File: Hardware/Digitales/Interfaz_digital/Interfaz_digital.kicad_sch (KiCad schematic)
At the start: 42 parts, among them J0 Screw_Terminal_01x09, J1-1 Screw_Terminal_01x01, J1-2 Screw_Terminal_01x01, J2-1 Screw_Terminal_01x01, J2-2 Screw_Terminal_01x01, J3-1 Screw_Terminal_01x01, J3-2 Screw_Terminal_01x01, J4-1 Screw_Terminal_01x01, J4-2 Screw_Terminal_01x01, J5-1 Screw_Terminal_01x01, J5-2 Screw_Terminal_01x01, J6-1 Screw_Terminal_01x01, J6-2 Screw_Terminal_01x01, J7-1 Screw_Terminal_01x01, J7-2 Screw_Terminal_01x01, J8-1 Screw_Terminal_01x01, J8-2 Screw_Terminal_01x01, J9 Screw_Terminal_01x10, U1 TLP521-1, U2 TLP521-1, U3 TLP521-1, U4 TLP521-1, U5 TLP521-1, U6 TLP521-1, U7 TLP521-1, U8 TLP521-1

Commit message: Referencias a los componentes de los circuitos
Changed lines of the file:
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@@
 	(text "Interfaz de señales digitales"
 		(exclude_from_sim no)
-		(at 212.344 172.72 0)
+		(at 235.204 173.228 0)
 		(effects
 			(font
@@
 			)
 		)
-		(property "Datasheet" "https://www.alldatasheet.com/html-pdf/32438/TOSHIBA/TLP521/245/1/TLP521.html"
+		(property "Datasheet" "https://docs.rs-online.com/d620/0900766b800287f7.pdf"
 			(at 160.02 102.87 0)
 			(effects
@@
 			)
 		)
-		(property "Datasheet" "https://www.alldatasheet.com/html-pdf/32438/TOSHIBA/TLP521/245/1/TLP521.html"
+		(property "Datasheet" "https://docs.rs-online.com/d620/0900766b800287f7.pdf"
 			(at 160.02 68.58 0)
 			(effects
@@
 			)
 		)
-		(property "Datasheet" "https://www.alldatasheet.com/html-pdf/32438/TOSHIBA/TLP521/245/1/TLP521.html"
+		(property "Datasheet" "https://docs.rs-online.com/d620/0900766b800287f7.pdf"
 			(at 160.02 156.21 0)
 			(effects
@@
 			)
 		)
-		(property "Datasheet" "https://www.alldatasheet.com/html-pdf/32438/TOSHIBA/TLP521/245/1/TLP521.html"
+		(property "Datasheet" "https://docs.rs-online.com/d620/0900766b800287f7.pdf"
 			(at 160.02 138.43 0)
 			(effects
@@
 			)
 		)
-		(property "Datasheet" "https://www.alldatasheet.com/html-pdf/32438/TOSHIBA/TLP521/245/1/TLP521.html"
+		(property "Datasheet" "https://docs.rs-online.com/d620/0900766b800287f7.pdf"
 			(at 160.02 33.02 0)
 			(effects
@@
 			)
 		)
-		(property "Datasheet" "https://www.alldatasheet.com/html-pdf/32438/TOSHIBA/TLP521/245/1/TLP521.html"
+		(property "Datasheet" "https://docs.rs-online.com/d620/0900766b800287f7.pdf"
 			(at 160.02 50.8 0)
 			(effects
@@
 			)
 		)
-		(property "Datasheet" "https://www.alldatasheet.com/html-pdf/32438/TOSHIBA/TLP521/245/1/TLP521.html"
+		(property "Datasheet" "https://docs.rs-online.com/d620/0900766b800287f7.pdf"
 			(at 160.02 120.65 0)
 			(effects
@@
 			)
 		)
-		(property "Datasheet" "https://www.alldatasheet.com/html-pdf/32438/TOSHIBA/TLP521/245/1/TLP521.html"
+		(property "Datasheet" "https://docs.rs-online.com/d620/0900766b800287f7.pdf"
 			(at 160.02 86.36 0)
 			(effects

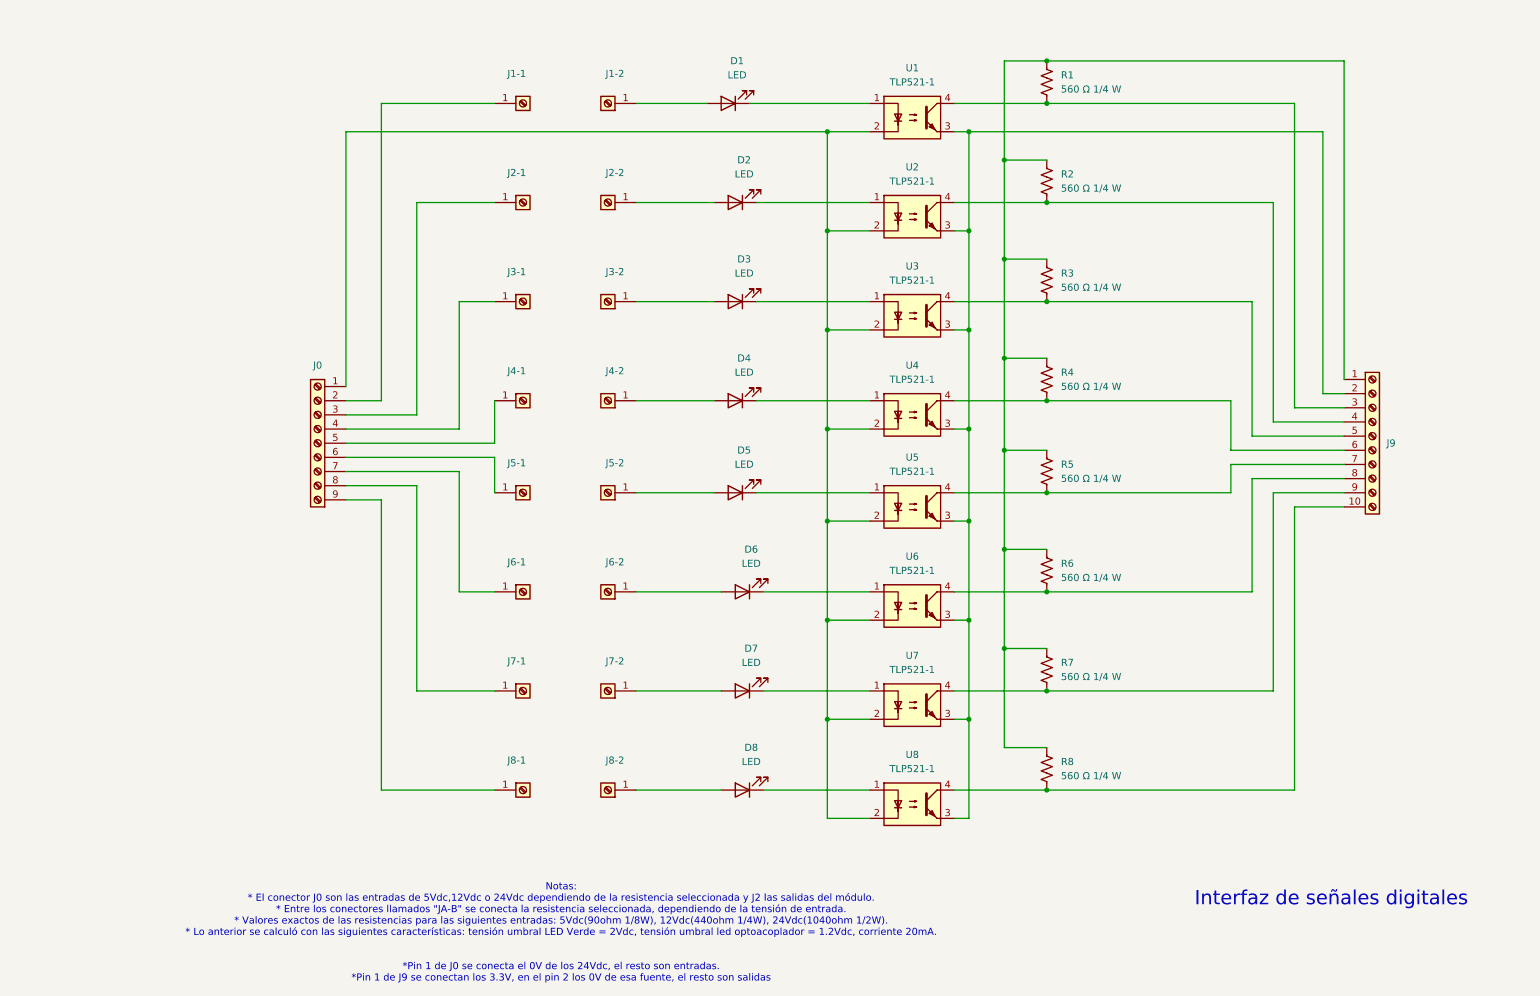
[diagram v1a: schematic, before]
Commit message: Corrección para el mensaje de alerta en estado manual
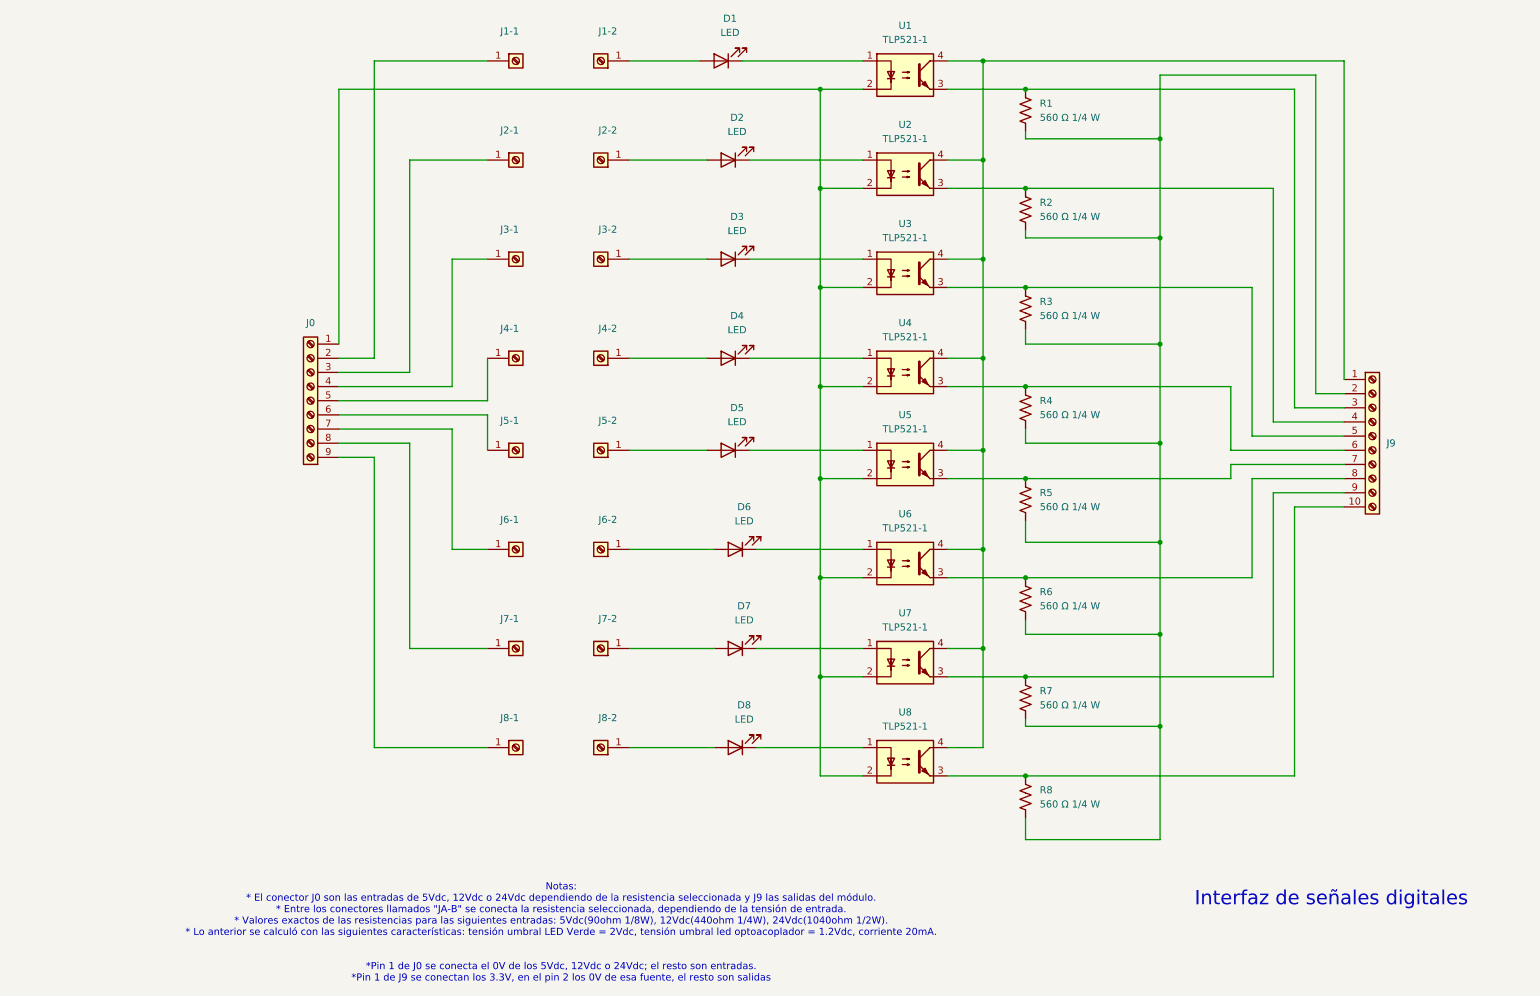
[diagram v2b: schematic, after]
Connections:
- new net: J9.7 (Pin_7), R5.1, U5.3
- new net: J9.1 (Pin_1), U1.4, U2.4, U3.4, U4.4, U5.4, U6.4, U7.4, U8.4
- new net: J9.5 (Pin_5), R3.1, U3.3
- new net: J9.10 (Pin_10), R8.1, U8.3
- new net: J9.2 (Pin_2), R1.2, R2.2, R3.2, R4.2, R5.2, R6.2, R7.2, R8.2
- new net: J9.8 (Pin_8), R6.1, U6.3
- new net: J9.9 (Pin_9), R7.1, U7.3
- new net: J9.3 (Pin_3), R1.1, U1.3
- new net: J9.4 (Pin_4), R2.1, U2.3
- new net: J9.6 (Pin_6), R4.1, U4.3
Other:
- note added: "Notas: * El conector J0 son las entradas de 5Vdc, 12Vdc o 24Vdc dependiendo de la resistencia seleccionada y J9 las salidas del módulo. * Entre los conectores llamados "JA-B" se conecta la resistencia seleccionada, dependiendo de la tensión de entrada. * Valores exactos de las resistencias para las siguientes entradas: 5Vdc(90ohm 1/8W), 12Vdc(440ohm 1/4W), 24Vdc(1040ohm 1/2W). * Lo anterior se ca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"
- note removed: "Notas: * El conector J0 son las entradas de 5Vdc,12Vdc o 24Vdc dependiendo de la resistencia seleccionada y J2 las salidas del módulo. * Entre los conectores llamados "JA-B" se conecta la resistencia seleccionada, dependiendo de la tensión de entrada. * Valores exactos de las resistencias para las siguientes entradas: 5Vdc(90ohm 1/8W), 12Vdc(440ohm 1/4W), 24Vdc(1040ohm 1/2W). * Lo anterior se cal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"
- moved on the sheet: D1, D2, D3, D4, D5, D6, D7, D8, J0, J1-1, J1-2, J2-1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

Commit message: Trabajando en el PCB de señales digitales
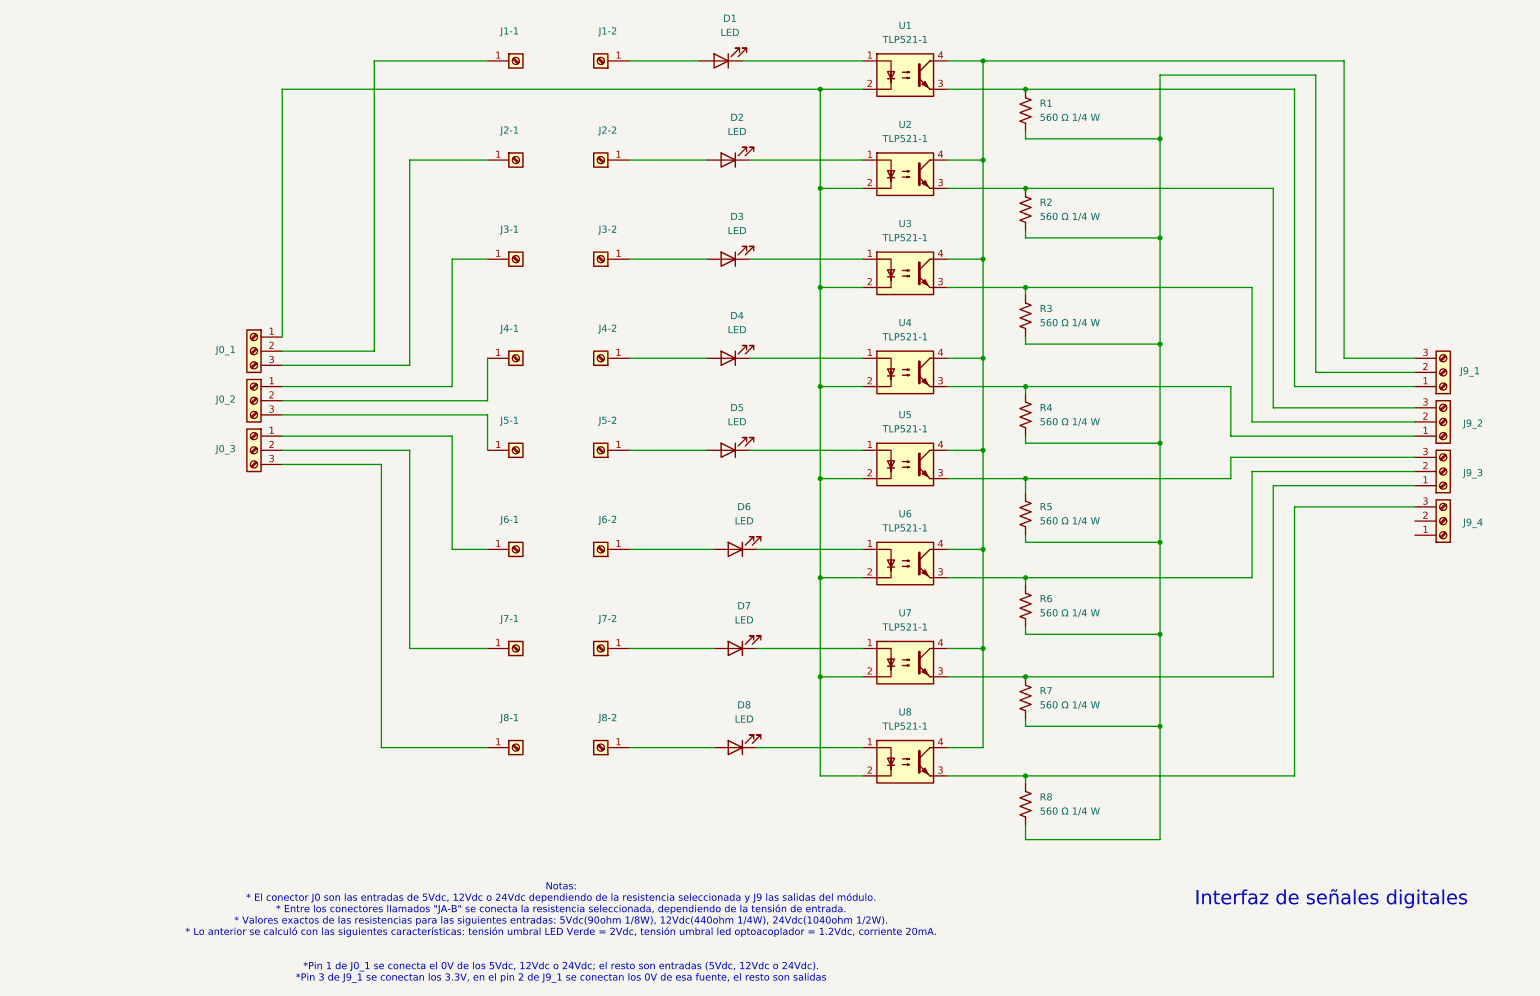
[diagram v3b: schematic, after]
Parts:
- removed J0: Screw_Terminal_01x09, symbol Connector:Screw_Terminal_01x09
- removed J9: Screw_Terminal_01x10, symbol Connector:Screw_Terminal_01x10
- added J0_1, J0_2, J0_3, J9_1, J9_2, J9_3, J9_4: Screw_Terminal_01x03, TerminalBlock_Phoenix:TerminalBlock_Phoenix_PT-1,5-3-3.5-H_1x03_P3.50mm_Horizontal, symbol Connector:Screw_Terminal_01x03
- D1, D2, D3, D4, D5, D6, D7, D8: footprint (none) -> LED_THT:LED_D4.0mm
- J1-1, J1-2, J2-1, J2-2, J3-1, J3-2, J4-1, J4-2, J5-1, J5-2, J6-1, J6-2, J7-1, J7-2, J8-1, J8-2: footprint (none) -> TerminalBlock_MetzConnect:TerminalBlock_MetzConnect_360271_1x01_Horizontal_ScrewM3.0_Boxed
- R1, R2, R3, R4, R5, R6, R7, R8: footprint (none) -> Resistor_THT:R_Axial_DIN0207_L6.3mm_D2.5mm_P10.16mm_Horizontal
- U1, U2, U3, U4, U5, U6, U7, U8: footprint (none) -> Package_DIP:DIP-4_W7.62mm
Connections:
- net at U1.2, U2.2, U3.2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: now also J0_1.1 (Pin_1)
- net at R5.1, U5.3: now also J9_3.3 (Pin_3)
- net at U1.4, U2.4, U3.4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: now also J9_1.3 (Pin_3)
- net at J7-1.1 (Pin_1): now also J0_3.2 (Pin_2)
- net at R3.1, U3.3: now also J9_2.2 (Pin_2)
- net at J3-1.1 (Pin_1): now also J0_2.1 (Pin_1)
- net at R8.1, U8.3: now also J9_4.3 (Pin_3)
- net at R1.2, R2.2, R3.2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: now also J9_1.2 (Pin_2)
- net at J6-1.1 (Pin_1): now also J0_3.1 (Pin_1)
- net at R6.1, U6.3: now also J9_3.2 (Pin_2)
- net at R7.1, U7.3: now also J9_3.1 (Pin_1)
- net at J8-1.1 (Pin_1): now also J0_3.3 (Pin_3)
- net at J1-1.1 (Pin_1): now also J0_1.2 (Pin_2)
- net at J2-1.1 (Pin_1): now also J0_1.3 (Pin_3)
- net at J4-1.1 (Pin_1): now also J0_2.2 (Pin_2)
- net at J5-1.1 (Pin_1): now also J0_2.3 (Pin_3)
- net at R1.1, U1.3: now also J9_1.1 (Pin_1)
- net at R2.1, U2.3: now also J9_2.3 (Pin_3)
- net at R4.1, U4.3: now also J9_2.1 (Pin_1)
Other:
- moved on the sheet: R3, R4, R5, R6, R8

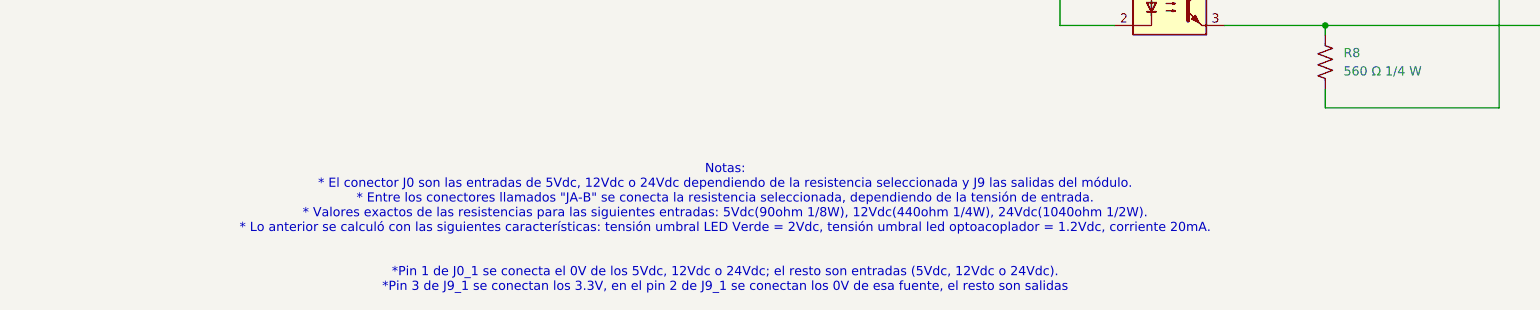
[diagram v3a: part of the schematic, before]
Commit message: Esquematicos de las PCB
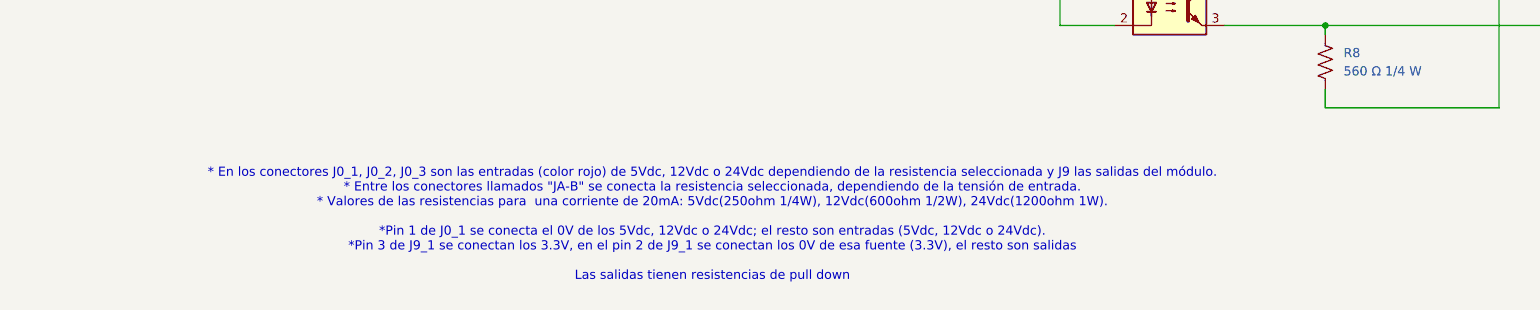
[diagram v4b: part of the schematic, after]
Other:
- note added: "* En los conectores J0_1, J0_2, J0_3 son las entradas (color rojo) de 5Vdc, 12Vdc o 24Vdc dependiendo de la resistencia seleccionada y J9 las salidas del módulo. * Entre los conectores llamados "JA-B" se conecta la resistencia seleccionada, dependiendo de la tensión de entrada. * Valores de las resistencias para una corriente de 20mA: 5Vdc(250ohm 1/4W), 12Vdc(600ohm 1/2W), 24Vdc(1200ohm 1W). *Pin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"
- note removed: "Notas: * El conector J0 son las entradas de 5Vdc, 12Vdc o 24Vdc dependiendo de la resistencia seleccionada y J9 las salidas del módulo. * Entre los conectores llamados "JA-B" se conecta la resistencia seleccionada, dependiendo de la tensión de entrada. * Valores exactos de las resistencias para las siguientes entradas: 5Vdc(90ohm 1/8W), 12Vdc(440ohm 1/4W), 24Vdc(1040ohm 1/2W). * Lo anterior se ca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"
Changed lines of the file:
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@@
 		)
 	)
-	(text "Notas: \n* El conector J0 son las entradas de 5Vdc, 12Vdc o 24Vdc dependiendo de la resistencia seleccionada y J9 las salidas del módulo. \n* Entre los conectores llamados \"JA-B\" se conecta la resistencia seleccionada, dependiendo de la tensión de entrada. \n* Valores exactos de las resistencias para las siguientes entradas: 5Vdc(90ohm 1/8W), 12Vdc(440ohm 1/4W), 24Vdc(1040ohm 1/2W). \n* Lo anterior se calculó con las siguientes características: tensión umbral LED Verde = 2Vdc, tensión umbral led optoacoplador = 1.2Vdc, corriente 20mA. \n\n\n*Pin 1 de J0_1 se conecta el 0V de los 5Vdc, 12Vdc o 24Vdc; el resto son entradas (5Vdc, 12Vdc o 24Vdc). \n*Pin 3 de J9_1 se conectan los 3.3V, en el pin 2 de J9_1 se conectan los 0V de esa fuente, el resto son salidas"
+	(text "* En los conectores J0_1, J0_2, J0_3 son las entradas (color rojo) de 5Vdc, 12Vdc o 24Vdc dependiendo de la resistencia seleccionada y J9 las salidas del módulo. \n* Entre los conectores llamados \"JA-B\" se conecta la resistencia seleccionada, dependiendo de la tensión de entrada. \n* Valores de las resistencias para  una corriente de 20mA: 5Vdc(250ohm 1/4W), 12Vdc(600ohm 1/2W), 24Vdc(1200ohm 1W). \n\n*Pin 1 de J0_1 se conecta el 0V de los 5Vdc, 12Vdc o 24Vdc; el resto son entradas (5Vdc, 12Vdc o 24Vdc). \n*Pin 3 de J9_1 se conectan los 3.3V, en el pin 2 de J9_1 se conectan los 0V de esa fuente (3.3V), el resto son salidas\n\nLas salidas tienen resistencias de pull down"
 		(exclude_from_sim no)
-		(at 97.028 179.324 0)
+		(at 95.25 178.816 0)
 		(effects
 			(font
